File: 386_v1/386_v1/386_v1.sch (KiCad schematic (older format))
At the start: 71 parts, among them U8 Conn_02x32_Odd_Even

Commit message: prepare for pcb 1.0
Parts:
- removed C? (x3): 100n, Capacitor_SMD:C_0805_2012Metric_Pad1.15x1.40mm_HandSolder, symbol Device:C_Small
- added U7A1, U8A1: Conn_02x32_Odd_Even, Connector_PinHeader_2.54mm:PinHeader_2x32_P2.54mm_Vertical, symbol Connector_Generic:Conn_02x32_Odd_Even
- U1, U2: renamed from U?; value 74LVC1G17 -> 74LVC1G17GW; footprint (none) -> Package_SO:TSOP-5_1.65x3.05mm_P0.95mm
- U3: renamed from U?; footprint (none) -> Package_QFP:LQFP-100_14x14mm_P0.5mm
- U7: renamed from U?; footprint (none) -> Connector_PinHeader_2.54mm:PinHeader_2x32_P2.54mm_Vertical
- U8: footprint (none) -> Connector_PinHeader_2.54mm:PinHeader_2x32_P2.54mm_Vertical
- gave numbers to parts that had none: 63
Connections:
- net +3V3: now also U7A1.3 (Pin_3), U7A1.4 (Pin_4), U8A1.3 (Pin_3), U8A1.4 (Pin_4)
- net +5V: now also U7A1.63 (Pin_63), U7A1.64 (Pin_64), U8A1.63 (Pin_63), U8A1.64 (Pin_64); no longer C1.2, C10.2, C11.2, C12.2, C2.2, C3.2, C4.2, C5.2, C6.2, C7.2, C8.2, C9.2, U1.3 (GND), U2.3 (GND), U3.11 (GND), U3.12 (GND), U3.13 (GND), U3.14 (GND), U3.2 (GND), U3.22 (GND), U3.35 (GND), U3.41 (GND), U3.49 (GND), U3.5 (GND), U3.50 (GND), U3.63 (GND), U3.67 (GND), U3.68 (GND), U3.77 (GND), U3.78 (GND), U3.85 (GND), U3.98 (GND), U7.2 (Pin_2), U7.6 (Pin_6), U7.61 (Pin_61), U7.62 (Pin_62), U8.1 (Pin_1), U8.2 (Pin_2), U8.5 (Pin_5), U8.6 (Pin_6), U8.62 (Pin_62)
- net F_A10_O: now also U8.15 (Pin_15), U8A1.15 (Pin_15); no longer U8.34 (Pin_34)
- net F_A11_O: now also U8.16 (Pin_16), U8A1.16 (Pin_16); no longer U8.32 (Pin_32)
- net F_A12_O: now also U8.17 (Pin_17), U8A1.17 (Pin_17); no longer U8.30 (Pin_30)
- net F_A13_O: now also U8.18 (Pin_18), U8A1.18 (Pin_18); no longer U8.28 (Pin_28)
- net F_A14_O: now also U8.19 (Pin_19), U8A1.19 (Pin_19); no longer U8.26 (Pin_26)
- net F_A15_O: now also U8.20 (Pin_20), U8A1.20 (Pin_20); no longer U8.24 (Pin_24)
- net F_A16_O: now also U8.21 (Pin_21), U8A1.21 (Pin_21); no longer U8.22 (Pin_22)
- net F_A17_O: now also U8.22 (Pin_22), U8A1.22 (Pin_22); no longer U8.20 (Pin_20)
- net F_A18_O: now also U8.23 (Pin_23), U8A1.23 (Pin_23); no longer U8.18 (Pin_18)
- net F_A19_O: now also U8.24 (Pin_24), U8A1.24 (Pin_24); no longer U8.16 (Pin_16)
- net F_A1_O: now also U8.51 (Pin_51), U8A1.51 (Pin_51); no longer U8.52 (Pin_52)
- net F_A20_O: now also U8.25 (Pin_25), U8A1.25 (Pin_25); no longer U8.14 (Pin_14)
- net F_A21_O: now also U8.26 (Pin_26), U8A1.26 (Pin_26); no longer U8.12 (Pin_12)
- net F_A22_O: now also U8.27 (Pin_27), U8A1.27 (Pin_27); no longer U8.10 (Pin_10)
- net F_A23_O: now also U8.28 (Pin_28), U8A1.28 (Pin_28); no longer U8.8 (Pin_8)
- net F_A2_O: now also U8.7 (Pin_7), U8A1.7 (Pin_7); no longer U8.50 (Pin_50)
- net F_A3_O: now also U8.8 (Pin_8), U8A1.8 (Pin_8); no longer U8.48 (Pin_48)
- net F_A4_O: now also U8.9 (Pin_9), U8A1.9 (Pin_9); no longer U8.46 (Pin_46)
- net F_A5_O: now also U8.10 (Pin_10), U8A1.10 (Pin_10); no longer U8.44 (Pin_44)
- net F_A6_O: now also U8.11 (Pin_11), U8A1.11 (Pin_11); no longer U8.42 (Pin_42)
- net F_A7_O: now also U8.12 (Pin_12), U8A1.12 (Pin_12); no longer U8.40 (Pin_40)
- net F_A8_O: now also U8.13 (Pin_13), U8A1.13 (Pin_13); no longer U8.38 (Pin_38)
- net F_A9_O: now also U8.14 (Pin_14), U8A1.14 (Pin_14); no longer U8.36 (Pin_36)
- net F_CLK_I: now also U8.48 (Pin_48), U8A1.48 (Pin_48); no longer U7.49 (Pin_49)
- net F_D0_IO: now also U8.44 (Pin_44), U8A1.44 (Pin_44); no longer U8.37 (Pin_37)
- net F_D10_IO: now also U8.34 (Pin_34), U8A1.34 (Pin_34); no longer U8.17 (Pin_17)
- net F_D11_IO: now also U8.33 (Pin_33), U8A1.33 (Pin_33); no longer U8.15 (Pin_15)
- net F_D12_IO: now also U8.32 (Pin_32), U8A1.32 (Pin_32); no longer U8.13 (Pin_13)
- net F_D13_IO: now also U8.31 (Pin_31), U8A1.31 (Pin_31); no longer U8.11 (Pin_11)
- net F_D14_IO: now also U8.30 (Pin_30), U8A1.30 (Pin_30); no longer U8.9 (Pin_9)
- net F_D15_IO: now also U8.29 (Pin_29), U8A1.29 (Pin_29); no longer U8.7 (Pin_7)
- net F_D1_IO: now also U8.43 (Pin_43), U8A1.43 (Pin_43); no longer U8.35 (Pin_35)
- net F_D2_IO: now also U8.42 (Pin_42), U8A1.42 (Pin_42); no longer U8.33 (Pin_33)
- net F_D3_IO: now also U8.41 (Pin_41), U8A1.41 (Pin_41); no longer U8.31 (Pin_31)
- net F_D4_IO: now also U8.40 (Pin_40), U8A1.40 (Pin_40); no longer U8.29 (Pin_29)
- net F_D5_IO: now also U8.39 (Pin_39), U8A1.39 (Pin_39); no longer U8.27 (Pin_27)
- net F_D6_IO: now also U8.38 (Pin_38), U8A1.38 (Pin_38); no longer U8.25 (Pin_25)
- net F_D7_IO: now also U8.37 (Pin_37), U8A1.37 (Pin_37); no longer U8.23 (Pin_23)
- net F_D8_IO: now also U8.36 (Pin_36), U8A1.36 (Pin_36); no longer U8.21 (Pin_21)
- net F_D9_IO: now also U8.35 (Pin_35), U8A1.35 (Pin_35); no longer U8.19 (Pin_19)
- net F_D~C~_O: now also U8.54 (Pin_54), U8A1.54 (Pin_54); no longer U8.41 (Pin_41)
- net F_HLDA_O: now also U8.45 (Pin_45), U8A1.45 (Pin_45); no longer U8.55 (Pin_55)
- net F_HOLD_I: now also U8.46 (Pin_46), U8A1.46 (Pin_46); no longer U8.53 (Pin_53)
- net F_INTR_I: now also U7.55 (Pin_55), U7A1.55 (Pin_55); no longer U8.57 (Pin_57)
- net F_M~IO~_O: now also U8.53 (Pin_53), U8A1.53 (Pin_53); no longer U8.43 (Pin_43)
- net F_NMI_I: now also U7.57 (Pin_57), U7A1.57 (Pin_57); no longer U8.59 (Pin_59)
- net F_PEREQ_I: now also U7.59 (Pin_59), U7A1.59 (Pin_59); no longer U7.57 (Pin_57)
- net F_RST_I: now also U8.58 (Pin_58), U8A1.58 (Pin_58); no longer U7.51 (Pin_51)
- net F_W~R~_O: now also U8.55 (Pin_55), U8A1.55 (Pin_55); no longer U8.39 (Pin_39)
- net F_~ADS~_O: now also U8.49 (Pin_49), U8A1.49 (Pin_49); no longer U8.47 (Pin_47)
- net F_~BHE~_O: now also U8.52 (Pin_52), U8A1.52 (Pin_52); no longer U8.54 (Pin_54)
- net F_~BLE~_O: now also U8.50 (Pin_50), U8A1.50 (Pin_50); no longer U8.56 (Pin_56)
- net F_~BUSY~_I: now also U8.59 (Pin_59), U8A1.59 (Pin_59); no longer U7.53 (Pin_53)
- net F_~ERROR~_I: now also U8.60 (Pin_60), U8A1.60 (Pin_60); no longer U7.55 (Pin_55)
- net F_~FLT~_I: now also U8.57 (Pin_57), U8A1.57 (Pin_57); no longer U7.59 (Pin_59)
- net F_~LOCK~_O: now also U8.56 (Pin_56), U8A1.56 (Pin_56); no longer U8.45 (Pin_45)
- net F_~READY~_I: now also U8.47 (Pin_47), U8A1.47 (Pin_47); no longer U8.51 (Pin_51)
- net GND: now reaches U7.1 (Pin_1), U7.5 (Pin_5), U8.61 (Pin_61)
- net GND: now also C1.2, C10.2, C11.2, C12.2, C2.2, C3.2, C4.2, C5.2, C6.2, C7.2, C8.2, C9.2, U1.3 (GND), U2.3 (GND), U3.11 (GND), U3.12 (GND), U3.13 (GND), U3.14 (GND), U3.2 (GND), U3.22 (GND), U3.35 (GND), U3.41 (GND), U3.49 (GND), U3.5 (GND), U3.50 (GND), U3.63 (GND), U3.67 (GND), U3.68 (GND), U3.77 (GND), U3.78 (GND), U3.85 (GND), U3.98 (GND), U7.2 (Pin_2), U7.6 (Pin_6), U7.61 (Pin_61), U7.62 (Pin_62), U8.1 (Pin_1), U8.2 (Pin_2), U8.5 (Pin_5), U8.6 (Pin_6), U8.62 (Pin_62), U7A1.1 (Pin_1), U7A1.2 (Pin_2), U7A1.5 (Pin_5), U7A1.6 (Pin_6), U7A1.61 (Pin_61), U7A1.62 (Pin_62), U8A1.1 (Pin_1), U8A1.2 (Pin_2), U8A1.5 (Pin_5), U8A1.6 (Pin_6), U8A1.61 (Pin_61), U8A1.62 (Pin_62)
- net 10: now reaches U7.10 (Pin_10)
- net 10: now also U7A1.10 (Pin_10)
- net 11: now reaches U7.11 (Pin_11)
- net 11: now also U7A1.11 (Pin_11)
- net 12: now reaches U7.12 (Pin_12)
- net 12: now also U7A1.12 (Pin_12)
- net 13: now reaches U7.13 (Pin_13)
- net 13: now also U7A1.13 (Pin_13)
- net 14: now reaches U7.14 (Pin_14)
- net 14: now also U7A1.14 (Pin_14)
- net 15: now reaches U7.15 (Pin_15)
- net 15: now also U7A1.15 (Pin_15)
- net 16: now reaches U7.16 (Pin_16)
- net 16: now also U7A1.16 (Pin_16)
- net 17: now reaches U7.17 (Pin_17)
- net 17: now also U7A1.17 (Pin_17)
- net 18: now reaches U7.18 (Pin_18)
- net 18: now also U7A1.18 (Pin_18)
- net 19: now reaches U7.19 (Pin_19)
- net 19: now also U7A1.19 (Pin_19)
- net 20: now reaches U7.20 (Pin_20)
- net 20: now also U7A1.20 (Pin_20)
- net 21: now reaches U7.21 (Pin_21)
- net 21: now also U7A1.21 (Pin_21)
- net 22: now reaches U7.22 (Pin_22)
- net 22: now also U7A1.22 (Pin_22)
- net 23: now reaches U7.23 (Pin_23)
- net 23: now also U7A1.23 (Pin_23)
- net 24: now reaches U7.24 (Pin_24)
- net 24: now also U7A1.24 (Pin_24)
- net 25: now reaches U7.25 (Pin_25)
- net 25: now also U7A1.25 (Pin_25)
- net 26: now reaches U7.26 (Pin_26)
- net 26: now also U7A1.26 (Pin_26)
- net 27: now reaches U7.27 (Pin_27)
- net 27: now also U7A1.27 (Pin_27)
- net 28: now reaches U7.28 (Pin_28)
- net 28: now also U7A1.28 (Pin_28)
- net 29: now reaches U7.29 (Pin_29)
- net 29: now also U7A1.29 (Pin_29)
- net 30: now reaches U7.30 (Pin_30)
- net 30: now also U7A1.30 (Pin_30)
- net 31: now reaches U7.31 (Pin_31)
- net 31: now also U7A1.31 (Pin_31)
- net 32: now reaches U7.32 (Pin_32)
- net 32: now also U7A1.32 (Pin_32)
- net 33: now reaches U7.33 (Pin_33)
- net 33: now also U7A1.33 (Pin_33)
- net 34: now reaches U7.34 (Pin_34)
- net 34: now also U7A1.34 (Pin_34)
- net 35: now reaches U7.35 (Pin_35)
- net 35: now also U7A1.35 (Pin_35)
- net 36: now reaches U7.36 (Pin_36)
- net 36: now also U7A1.36 (Pin_36)
- net 37: now reaches U7.37 (Pin_37)
- net 37: now also U7A1.37 (Pin_37)
- net 38: now reaches U7.38 (Pin_38)
- net 38: now also U7A1.38 (Pin_38)
- net 39: now reaches U7.39 (Pin_39)
- net 39: now also U7A1.39 (Pin_39)
- net 40: now reaches U7.40 (Pin_40)
- net 40: now also U7A1.40 (Pin_40)
- net 41: now reaches U7.41 (Pin_41)
- net 41: now also U7A1.41 (Pin_41)
- net 42: now reaches U7.42 (Pin_42)
- net 42: now also U7A1.42 (Pin_42)
- net 43: now reaches U7.43 (Pin_43)
- net 43: now also U7A1.43 (Pin_43)
- net 44: now reaches U7.44 (Pin_44)
- net 44: now also U7A1.44 (Pin_44)
- net 45: now reaches U7.45 (Pin_45)
- net 45: now also U7A1.45 (Pin_45)
- net 46: now reaches U7.46 (Pin_46)
- net 46: now also U7A1.46 (Pin_46)
- net 47: now reaches U7.47 (Pin_47)
- net 47: now also U7A1.47 (Pin_47)
- net 48: now reaches U7.48 (Pin_48)
- net 48: now also U7A1.48 (Pin_48)
- net 50: now reaches U7.50 (Pin_50)
- net 50: now also U7A1.50 (Pin_50)
- net 52: now reaches U7.52 (Pin_52)
- net 52: now also U7A1.52 (Pin_52)
- net 54: now reaches U7.54 (Pin_54)
- net 54: now also U7A1.54 (Pin_54)
- net 56: now reaches U7.56 (Pin_56)
- net 56: now also U7A1.56 (Pin_56)
- net 58: now reaches U7.58 (Pin_58)
- net 58: now also U7A1.58 (Pin_58)
- net 60: now reaches U7.60 (Pin_60)
- net 60: now also U7A1.60 (Pin_60)
- net 7: now reaches U7.7 (Pin_7)
- net 7: now also U7A1.7 (Pin_7)
- net 8: now reaches U7.8 (Pin_8)
- net 8: now also U7A1.8 (Pin_8)
- net 9: now reaches U7.9 (Pin_9)
- net 9: now also U7A1.9 (Pin_9)
- new net 49: U7.49 (Pin_49), U7A1.49 (Pin_49)
- new net 51: U7.51 (Pin_51), U7A1.51 (Pin_51)
- new net 53: U7.53 (Pin_53), U7A1.53 (Pin_53)
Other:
- moved on the sheet: R1, R10, R11, R12, R13, R14, R15, R16, R17, R18, R19, R2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

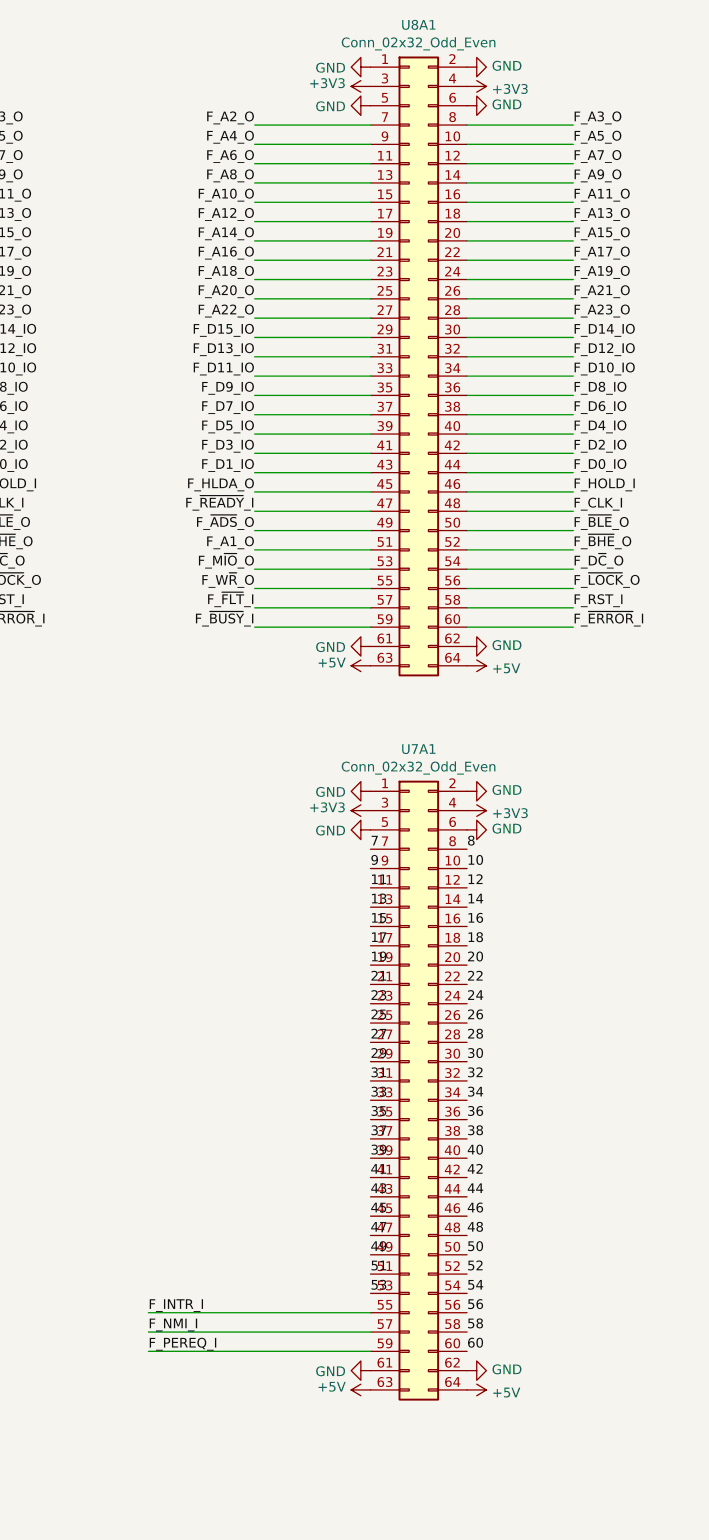
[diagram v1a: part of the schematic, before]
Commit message: use stack-trough connector
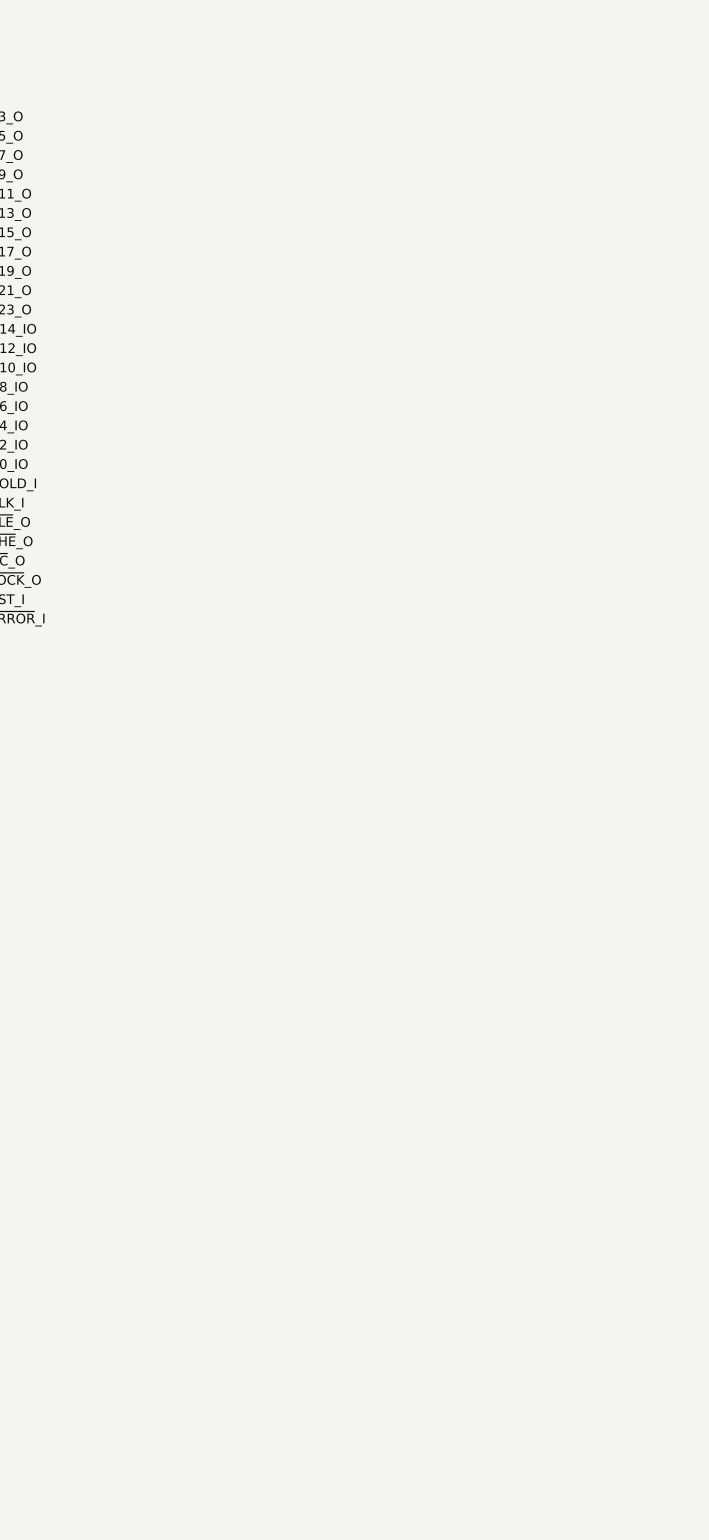
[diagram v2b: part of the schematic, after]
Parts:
- removed U7A1, U8A1: Conn_02x32_Odd_Even, Connector_PinHeader_2.54mm:PinHeader_2x32_P2.54mm_Vertical, symbol Connector_Generic:Conn_02x32_Odd_Even

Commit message: update
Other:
- moved on the sheet: C1, C10, C11, C12, C2, C3, C4, C5, C6, C7, C8, C9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
